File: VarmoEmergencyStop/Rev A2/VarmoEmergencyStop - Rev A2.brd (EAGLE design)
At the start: 95 x 25 mm, 7 parts, among them X1 NC3MAV, X2 NC3FAV2, X3 NC3MAV

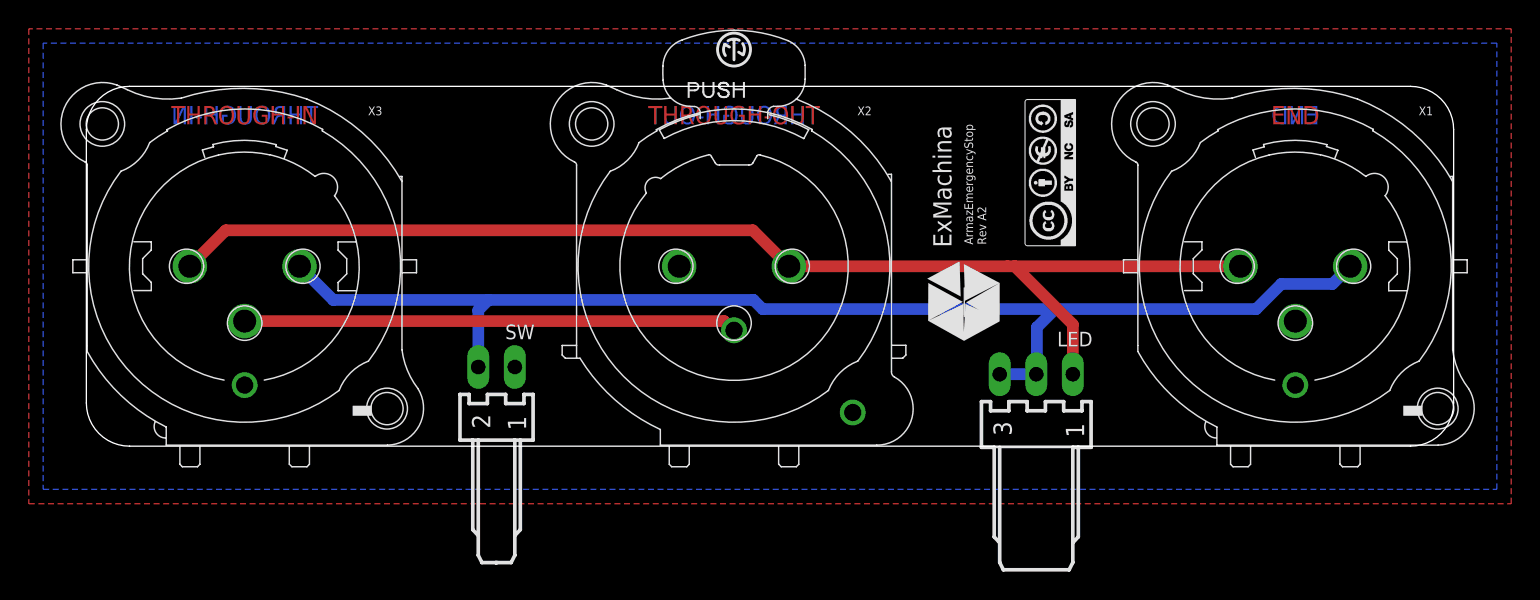
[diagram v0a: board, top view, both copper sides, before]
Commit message: Update VarmoEmergencyStop - Rev A2
* Add ExMachina logo to the back of the board
* Resize the board to the minimal
* Fix clearance issue
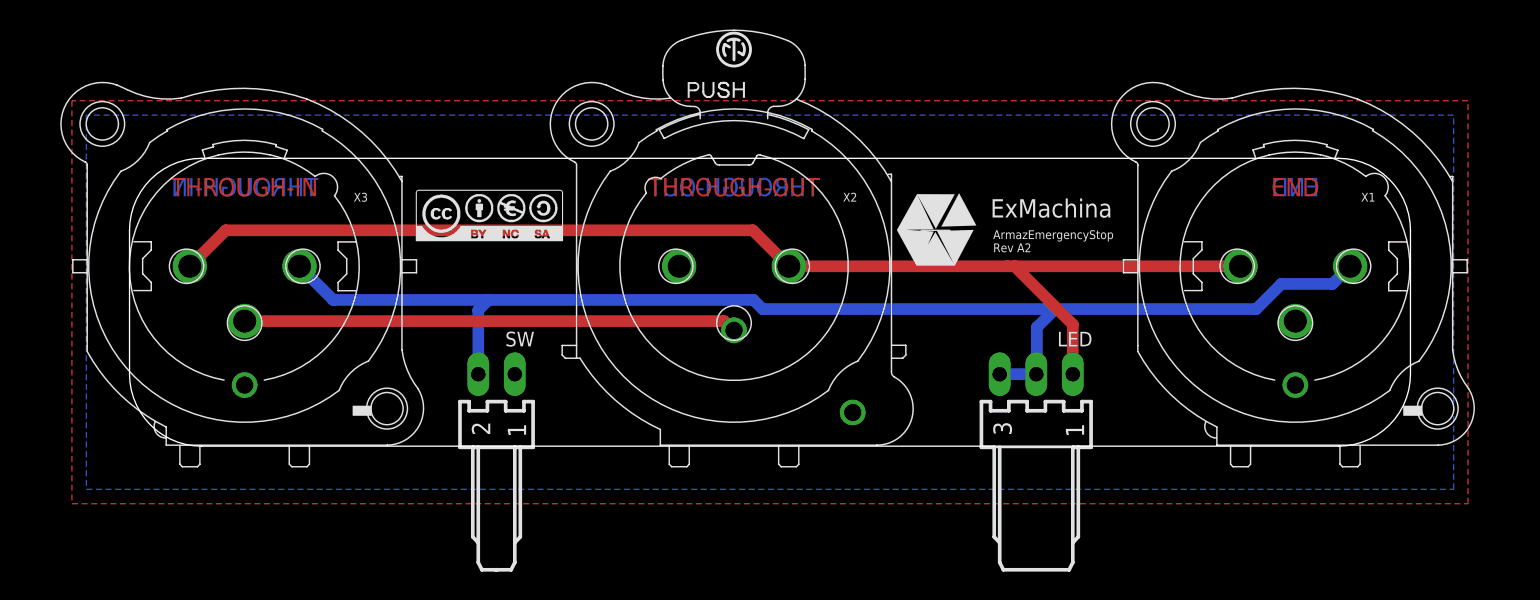
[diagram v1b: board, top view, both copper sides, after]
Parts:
- added U$3: EXMACHINA-LOGO-NAME, exmachina:EXM-LOGO-BASELINE
- moved U$2 39.1 mm to (28.0, 16.0), turned to 0 degrees
- moved U$1 5.39 mm to (59.0, 15.0), turned to 0 degrees
- moved SW 0.50 mm to (28.5, 5.00)
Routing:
- net ES-END: track 88.0 -> 88.5 mm
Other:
- board size 95 x 25 mm -> 89 x 20 mm
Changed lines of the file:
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@@
 <setting verticaltext="up"/>
 </settings>
-<grid distance="25" unitdist="mil" unit="mil" style="dots" multiple="2" display="yes" altdistance="5" altunitdist="mil" altunit="mil"/>
+<grid distance="1" unitdist="mm" unit="mm" style="dots" multiple="2" display="yes" altdistance="5" altunitdist="mil" altunit="mil"/>
 <layers>
 <layer number="1" name="Top" color="16" fill="1" visible="yes" active="yes"/>
@@
 <layer number="20" name="Dimension" color="7" fill="1" visible="yes" active="yes"/>
 <layer number="21" name="tPlace" color="55" fill="1" visible="yes" active="yes"/>
-<layer number="22" name="bPlace" color="54" fill="1" visible="no" active="yes"/>
+<layer number="22" name="bPlace" color="54" fill="1" visible="yes" active="yes"/>
 <layer number="23" name="tOrigins" color="15" fill="1" visible="yes" active="yes"/>
-<layer number="24" name="bOrigins" color="15" fill="1" visible="no" active="yes"/>
+<layer number="24" name="bOrigins" color="15" fill="1" visible="yes" active="yes"/>
 <layer number="25" name="tNames" color="55" fill="1" visible="yes" active="yes"/>
-<layer number="26" name="bNames" color="54" fill="1" visible="no" active="yes"/>
+<layer number="26" name="bNames" color="54" fill="1" visible="yes" active="yes"/>
 <layer number="27" name="tValues" color="53" fill="1" visible="yes" active="yes"/>
-<layer number="28" name="bValues" color="52" fill="1" visible="no" active="yes"/>
+<layer number="28" name="bValues" color="52" fill="1" visible="yes" active="yes"/>
 <layer number="29" name="tStop" color="7" fill="3" visible="no" active="yes"/>
 <layer number="30" name="bStop" color="7" fill="6" visible="no" active="yes"/>
@@
 <layer number="50" name="dxf" color="7" fill="1" visible="no" active="no"/>
 <layer number="51" name="tDocu" color="55" fill="1" visible="yes" active="yes"/>
-<layer number="52" name="bDocu" color="54" fill="1" visible="no" active="yes"/>
+<layer number="52" name="bDocu" color="54" fill="1" visible="yes" active="yes"/>
 <layer number="53" name="tGND_GNDA" color="7" fill="1" visible="no" active="no"/>
 <layer number="54" name="bGND_GNDA" color="7" fill="1" visible="no" active="no"/>
@@
 <board>
 <plain>
-<wire x1="92" y1="25" x2="3" y2="25" width="0" layer="20"/>
-<wire x1="3" y1="25" x2="0" y2="22" width="0" layer="20" curve="90"/>
-<wire x1="0" y1="22" x2="0" y2="3" width="0" layer="20"/>
-<wire x1="0" y1="3" x2="3" y2="0" width="0" layer="20" curve="90"/>
-<wire x1="3" y1="0" x2="92" y2="0" width="0" layer="20"/>
-<wire x1="92" y1="0" x2="95" y2="3" width="0" layer="20" curve="90"/>
-<wire x1="95" y1="3" x2="95" y2="22" width="0" layer="20"/>
-<wire x1="95" y1="22" x2="92" y2="25" width="0" layer="20" curve="90"/>
-<dimension x1="11" y1="12.5" x2="45" y2="12.5" x3="28" y3="31" textsize="1.778" layer="47" extoffset="3"/>
-<dimension x1="45" y1="12.5" x2="84" y2="12.5" x3="64.5" y3="31" textsize="1.778" layer="47" extoffset="3"/>
-<text x="84" y="23" size="1.27" layer="1" ratio="10" align="center">END</text>
-<text x="84" y="23" size="1.27" layer="16" ratio="10" rot="MR0" align="center">END</text>
-<text x="45" y="23" size="1.27" layer="1" ratio="10" align="center">THROUGH-OUT</text>
-<text x="11" y="23" size="1.27" layer="1" ratio="10" align="center">THROUGH-IN</text>
-<text x="11" y="23" size="1.27" layer="16" ratio="10" rot="MR0" align="center">THROUGH-IN</text>
-<text x="45" y="23" size="1.27" layer="16" ratio="10" rot="MR0" align="center">THROUGH-OUT</text>
-<text x="61" y="14" size="0.6096" layer="21" ratio="10" rot="R90" align="top-left">ArmazEmergencyStop
+<wire x1="92" y1="5" x2="92" y2="15" width="0" layer="20"/>
+<wire x1="92" y1="15" x2="87" y2="20" width="0" layer="20" curve="90"/>
+<wire x1="87" y1="20" x2="8" y2="20" width="0" layer="20"/>
+<wire x1="8" y1="20" x2="3" y2="15" width="0" layer="20" curve="90"/>
+<wire x1="3" y1="15" x2="3" y2="5" width="0" layer="20"/>
+<wire x1="3" y1="5" x2="8" y2="0" width="0" layer="20" curve="90"/>
+<wire x1="8" y1="0" x2="87" y2="0" width="0" layer="20"/>
+<wire x1="87" y1="0" x2="92" y2="5" width="0" layer="20" curve="90"/>
+<dimension x1="11" y1="12.5" x2="45" y2="12.5" x3="28" y3="26" textsize="1.778" layer="47" extoffset="3"/>
+<dimension x1="45" y1="12.5" x2="84" y2="12.5" x3="64.5" y3="26" textsize="1.778" layer="47" extoffset="3"/>
+<text x="84" y="18" size="1.27" layer="1" ratio="10" align="center">END</text>
+<text x="84" y="18" size="1.27" layer="16" ratio="10" rot="MR0" align="center">END</text>
+<text x="45" y="18" size="1.27" layer="1" ratio="10" align="center">THROUGH-OUT</text>
+<text x="11" y="18" size="1.27" layer="1" ratio="10" align="center">THROUGH-IN</text>
+<text x="11" y="18" size="1.27" layer="16" ratio="10" rot="MR0" align="center">THROUGH-IN</text>
+<text x="45" y="18" size="1.27" layer="16" ratio="10" rot="MR0" align="center">THROUGH-OUT</text>
+<text x="63" y="15" size="0.6096" layer="21" ratio="10" align="top-left">ArmazEmergencyStop
+Rev A2</text>
+<text x="66" y="15" size="0.6096" layer="22" ratio="10" rot="MR0" align="top-left">ArmazEmergencyStop
 Rev A2</text>
 </plain>
@@
 </autorouter>
 <elements>
-<element name="SW" library="con-molex" package="7395-02" value="22-05-7028-02" x="28.5" y="5.5" smashed="yes">
-<attribute name="OC_FARNELL" value="9731601" x="28.5" y="5.5" size="1.778" layer="27" display="off"/>
-<attribute name="OC_NEWARK" value="unknown" x="28.5" y="5.5" size="1.778" layer="27" display="off"/>
-<attribute name="MPN" value="" x="28.5" y="5.5" size="1.778" layer="27" display="off"/>
-<attribute name="MF" value="" x="28.5" y="5.5" size="1.778" layer="27" display="off"/>
-<attribute name="NAME" x="31.1401" y="8.4479" size="1.016" layer="21" ratio="10" rot="R180"/>
+<element name="SW" library="con-molex" package="7395-02" value="22-05-7028-02" x="28.5" y="5" smashed="yes">
+<attribute name="OC_FARNELL" value="9731601" x="28.5" y="5" size="1.778" layer="27" display="off"/>
+<attribute name="OC_NEWARK" value="unknown" x="28.5" y="5" size="1.778" layer="27" display="off"/>
+<attribute name="MPN" value="" x="28.5" y="5" size="1.778" layer="27" display="off"/>
+<attribute name="MF" value="" x="28.5" y="5" size="1.778" layer="27" display="off"/>
+<attribute name="NAME" x="31.1401" y="7.9479" size="1.016" layer="21" ratio="10" rot="R180"/>
 </element>
 <element name="X1" library="con-neutrik_ag" package="NC3MAV" value="NC3MAV" x="84" y="12.5" smashed="yes">
@@
 <attribute name="MPN" value="NC3MAV" x="84" y="12.5" size="1.778" layer="27" display="off"/>
 <attribute name="MF" value="FARNELL" x="84" y="12.5" size="1.778" layer="27" display="off"/>
-<attribute name="NAME" x="92.57" y="22.99" size="0.6096" layer="21"/>
+<attribute name="NAME" x="88.57" y="16.99" size="0.6096" layer="21"/>
 </element>
 <element name="X2" library="con-neutrik_ag" package="NC3FAV2" value="NC3FAV2" x="45" y="12.5" smashed="yes">
@@
 <attribute name="MPN" value="NC3FAV2" x="45" y="12.5" size="1.778" layer="27" display="off"/>
 <attribute name="MF" value="NEUTRIK" x="45" y="12.5" size="1.778" layer="27" display="off"/>
-<attribute name="NAME" x="53.57" y="22.99" size="0.6096" layer="21"/>
+<attribute name="NAME" x="52.57" y="16.99" size="0.6096" layer="21"/>
 </element>
 <element name="X3" library="con-neutrik_ag" package="NC3MAV" value="NC3MAV" x="11" y="12.5" smashed="yes">
@@
 <attribute name="MPN" value="NC3MAV" x="11" y="12.5" size="1.778" layer="27" display="off"/>
 <attribute name="MF" value="FARNELL" x="11" y="12.5" size="1.778" layer="27" display="off"/>
-<attribute name="NAME" x="19.57" y="22.99" size="0.6096" layer="21"/>
+<attribute name="NAME" x="18.57" y="16.99" size="0.6096" layer="21"/>
 </element>
-<element name="U$1" library="exmachina" package="EXM-LOGO-BASELINE" value="EXMACHINA-LOGO-NAME" x="61" y="10" rot="R90"/>
-<element name="U$2" library="cc-by-sa" package="CC-BY-NC-SA" value="CC-BY-NC-SA" x="67" y="19" rot="R90"/>
+<element name="U$1" library="exmachina" package="EXM-LOGO-BASELINE" value="EXMACHINA-LOGO-NAME" x="59" y="15"/>
+<element name="U$2" library="cc-by-sa" package="CC-BY-NC-SA" value="CC-BY-NC-SA" x="28" y="16"/>
 <element name="LED" library="con-molex" package="7395-03" value="22-05-7038-03" x="66" y="5" smashed="yes">
 <attribute name="OC_NEWARK" value="unknown" x="66" y="5" size="1.778" layer="27" display="off"/>
@@
 <attribute name="NAME" x="69.9101" y="7.9479" size="1.016" layer="21" ratio="10" rot="R180"/>
 </element>
+<element name="U$3" library="exmachina" package="EXM-LOGO-BASELINE" value="EXMACHINA-LOGO-NAME" x="70" y="15" rot="MR0"/>
 </elements>
 <signals>
 <signal name="+5V-END" class="1">
 <polygon width="0.8128" layer="1" isolate="0.3048">
-<vertex x="-4" y="-4"/>
-<vertex x="99" y="-4"/>
-<vertex x="99" y="29"/>
-<vertex x="-4" y="29"/>
+<vertex x="-1" y="-4"/>
+<vertex x="96" y="-4"/>
+<vertex x="96" y="24"/>
+<vertex x="-1" y="24"/>
 </polygon>
 <contactref element="X2" pad="2"/>
@@
 <contactref element="X2" pad="G"/>
 <polygon width="0.8128" layer="16" isolate="0.3048">
-<vertex x="-3" y="-3"/>
-<vertex x="98" y="-3"/>
-<vertex x="98" y="28"/>
-<vertex x="-3" y="28"/>
+<vertex x="0" y="-3"/>
+<vertex x="95" y="-3"/>
+<vertex x="95" y="23"/>
+<vertex x="0" y="23"/>
 </polygon>
 </signal>
@@
 <wire x1="27.94" y1="10.16" x2="17.15" y2="10.16" width="0.8128" layer="16"/>
 <wire x1="17.15" y1="10.16" x2="14.81" y2="12.5" width="0.8128" layer="16"/>
-<wire x1="27.23" y1="5.5" x2="27.23" y2="9.45" width="0.8128" layer="16"/>
+<wire x1="27.23" y1="5" x2="27.23" y2="9.45" width="0.8128" layer="16"/>
 <wire x1="27.23" y1="9.45" x2="27.94" y2="10.16" width="0.8128" layer="16"/>
 <wire x1="66.04" y1="8.255" x2="66.04" y2="5.04" width="0.8128" layer="16"/>
